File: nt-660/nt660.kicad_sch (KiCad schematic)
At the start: 159 parts, among them J1 USB_mini_micro_B, J2 ISP, K1 KEYSW, K10 KEYSW, K11 KEYSW, K12 KEYSW, K13 KEYSW, K14 KEYSW, K15 KEYSW, K16 KEYSW, K17 KEYSW, K18 KEYSW, K19 KEYSW, K2 KEYSW, K20 KEYSW, K21 KEYSW, K22 KEYSW, K23 KEYSW, K24 KEYSW, K25 KEYSW, K26 KEYSW, K27 KEYSW, K28 KEYSW, K29 KEYSW, K3 KEYSW, K30 KEYSW, K31 KEYSW, K32 KEYSW, K33 KEYSW, K34 KEYSW, K35 KEYSW, K36 KEYSW, K37 KEYSW, K38 KEYSW, K39 KEYSW, K4 KEYSW, K40 KEYSW, K41 KEYSW, K42 KEYSW, K43 KEYSW, K44 KEYSW, K44-1 KEYSW, K46 KEYSW, K46-1 KEYSW, K47 KEYSW, K48 KEYSW, K49 KEYSW, K5 KEYSW, K50 KEYSW, K51 KEYSW, K52 KEYSW, K53 KEYSW, K54 KEYSW, K55 KEYSW, K56 KEYSW, K57 KEYSW, K58 KEYSW, K59 KEYSW, K6 KEYSW, K61 KEYSW, K62 KEYSW, K62-1 KEYSW, K63 KEYSW, K63-1 KEYSW, K67 KEYSW, K67-1 KEYSW, K7 KEYSW, K70 KEYSW, K71 KEYSW, K72 KEYSW, K73 KEYSW, K74 KEYSW, K75 KEYSW, K8 KEYSW, K9 KEYSW, SW1 Reset, U1 ATmega32U4, U2 USBLC6-2SC6, X1 CSTNE16M0V530000R0

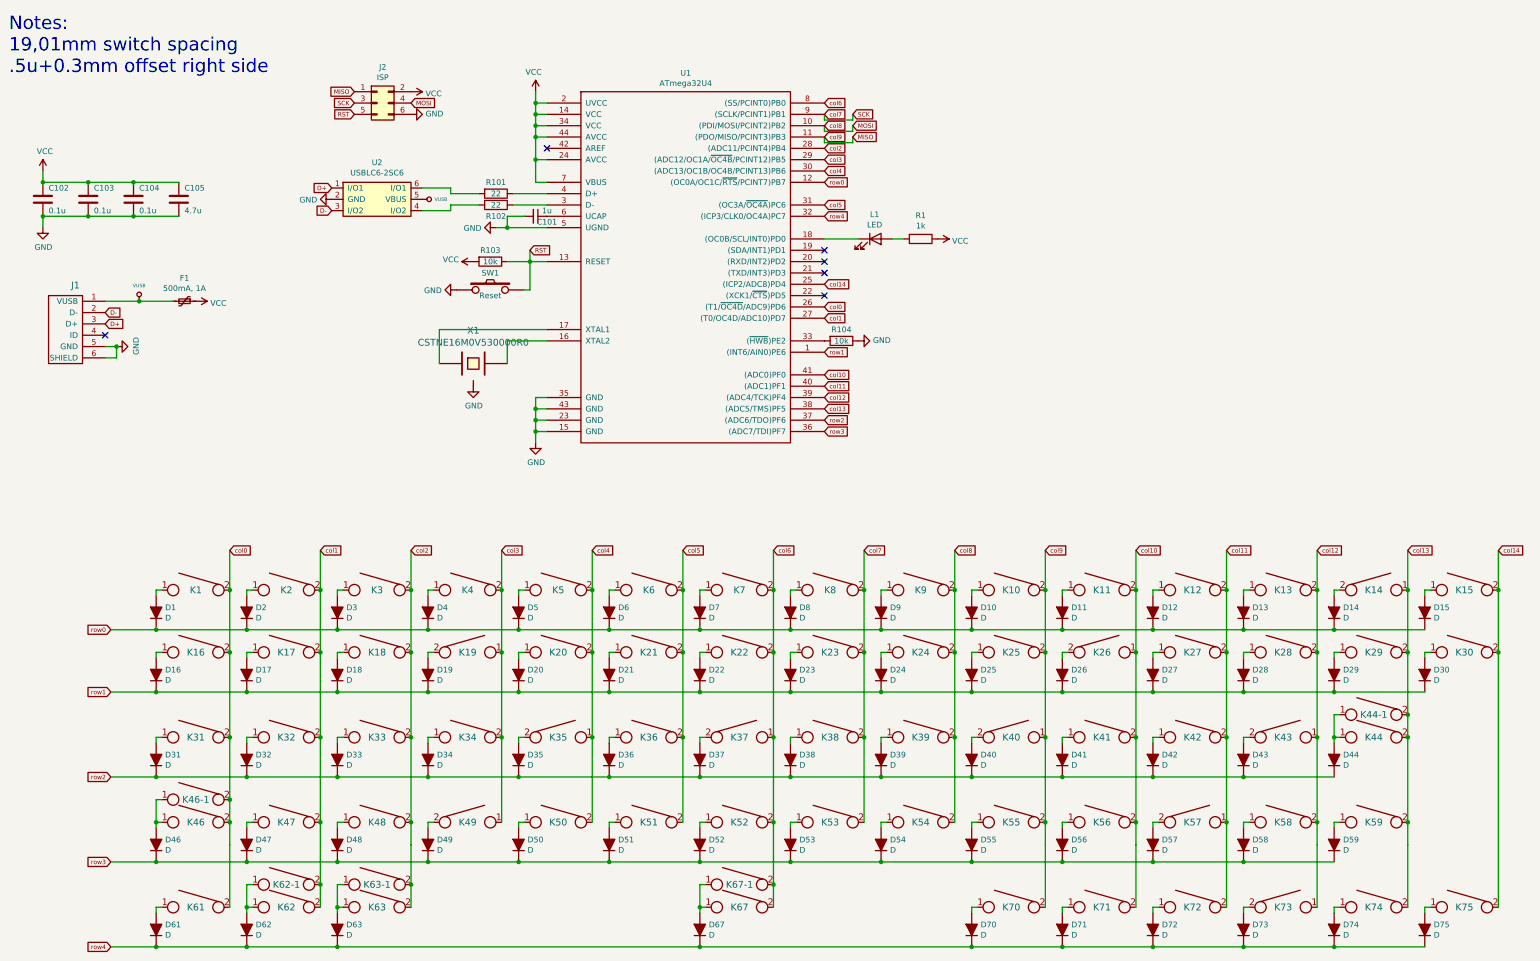
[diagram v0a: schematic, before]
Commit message: Add rotary encoder and change USB footprint to THT
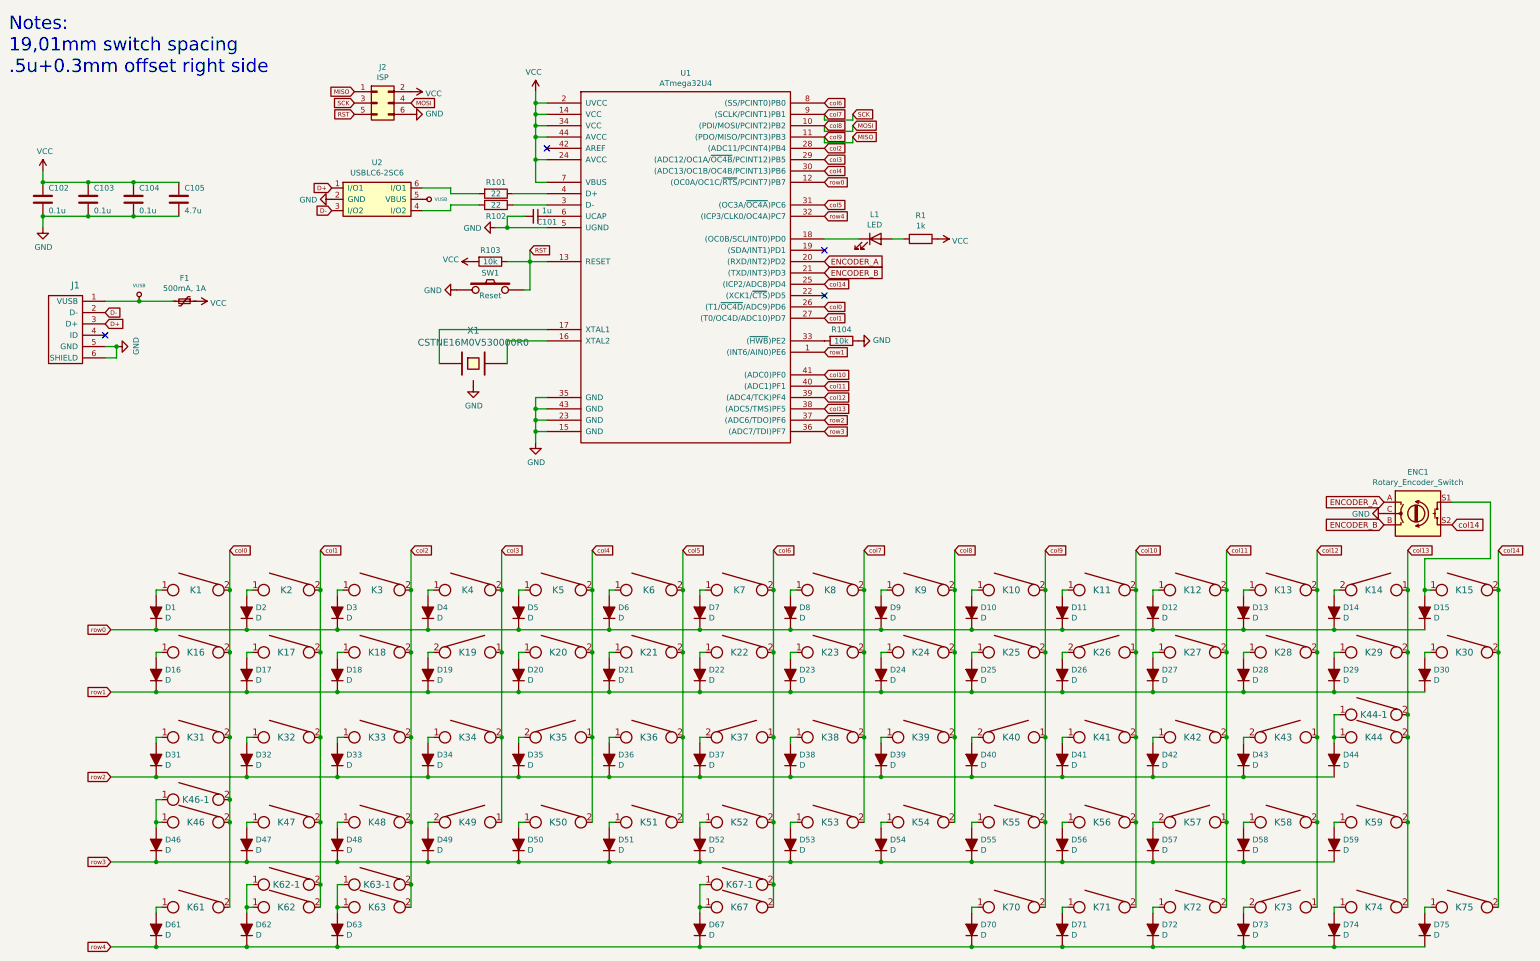
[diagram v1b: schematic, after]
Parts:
- added ENC1: Rotary_Encoder_Switch, Rotary_Encoder:RotaryEncoder_Alps_EC11E-Switch_Vertical_H20mm, symbol Device:Rotary_Encoder_Switch
- D1, D10, D11, D12, D13, D14, D15, D16, D17, D18, D19, D2, D20, D21, D22, D23, D24, D25, D26, D27, D28, D29, D3, D30, D31, D32, D33, D34, D35, D36, D37, D38, D39, D4, D40, D41, D42, D43, D44, D46, D47, D48, D49, D5, D50, D51, D52, D53, D54, D55, D56, D57, D58, D59, D6, D61, D62, D63, D67, D7, D70, D71, D72, D73, D74, D75, D8, D9: footprint Keeb_components:D_0805 -> Diode_SMD:D_SOD-123
- J1: footprint Keeb_components:U-M-M5DD-W-1 -> .github:USB-Mini-B_ LCSC-C46398
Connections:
- net GND: now also ENC1.C
- net col14: now also ENC1.S2
- net ENCODER_A: now reaches U1.20 ((RXD/INT2)PD2)
- net ENCODER_A: now also ENC1.A
- net ENCODER_B: now reaches U1.21 ((TXD/INT3)PD3)
- net ENCODER_B: now also ENC1.B
- net at D15.2 (A), K15.1: now also ENC1.S1
- no-connect marks 6 -> 4
